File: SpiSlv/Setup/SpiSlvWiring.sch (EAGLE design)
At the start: 4 parts

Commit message: SpiSlv: changes for ^9
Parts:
- removed BM3: (no value), Documentation:RPUNO
- added BM1: (no value), Documentation:RPUNO
- D1: value GN -> RD
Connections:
- removed net 12V_SLA: BM3.BAT
- removed net 21V@200MA: BM3.PV
- removed net MOSI-MISO-SCK: BM3.SPI, U$1.SPI
- new net 12V8: BM1.PWR
- new net MOSI-MISO-SCK-CE0: BM1.SPI, U$1.SPI
- net !SS: now also BM1.ADC2_16, BM1.DIO10; no longer BM3.DIO10, BM3.DIO3
- net 5V-SMPS-ON-RPUPI: now also BM1.SHLD_VOUT; no longer BM3.SHLD_VOUT
- net N$1: now also BM1.CS0_EN5; no longer BM3.20MA@2
- net N$2: now also BM1.0V@3; no longer BM3.DIO4
- net N$5: now also BM1.RX; no longer BM3.RX
- net N$8: now also BM1.TX; no longer BM3.TX
- net SDA-SCL: now also BM1.I2C; no longer BM3.I2C
- net THRU-74LVC07: now also BM1.!RESET; no longer BM3.!RESET
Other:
- note added: "Note: nSS is active low hack: DIO16 used to operate nSS"
- note added: "hack"
- note removed: "Note: nSS is active low SPI will not work until it is active."
- moved on the sheet: D1

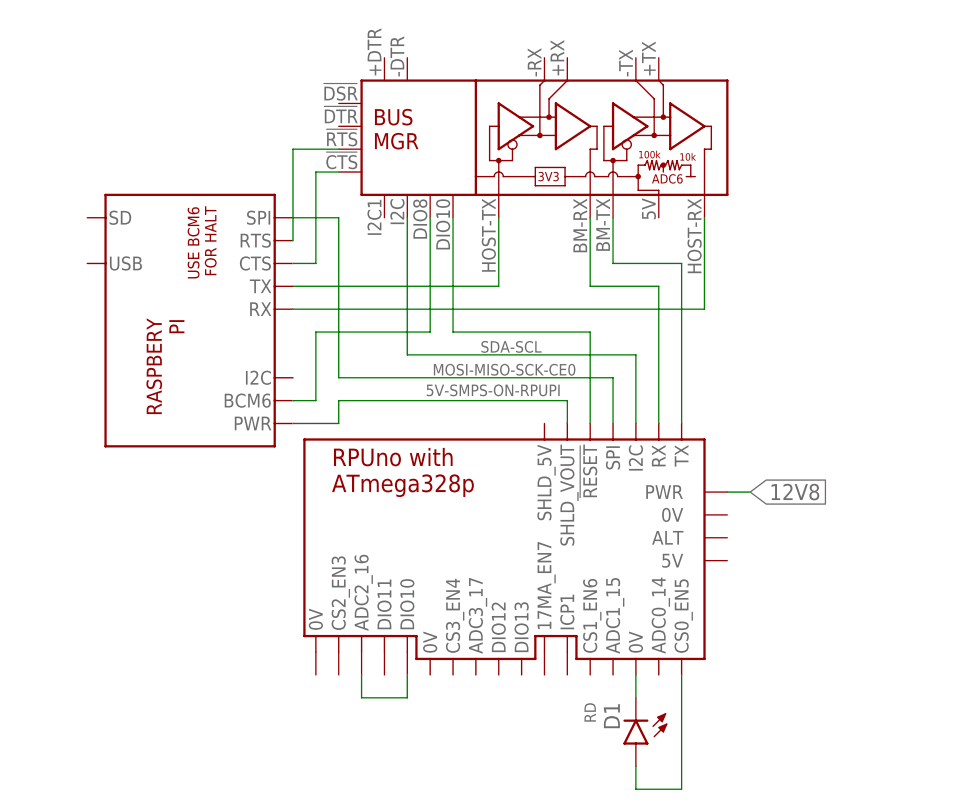
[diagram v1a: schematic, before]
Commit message: SpiSlv: remove ADC2 notes
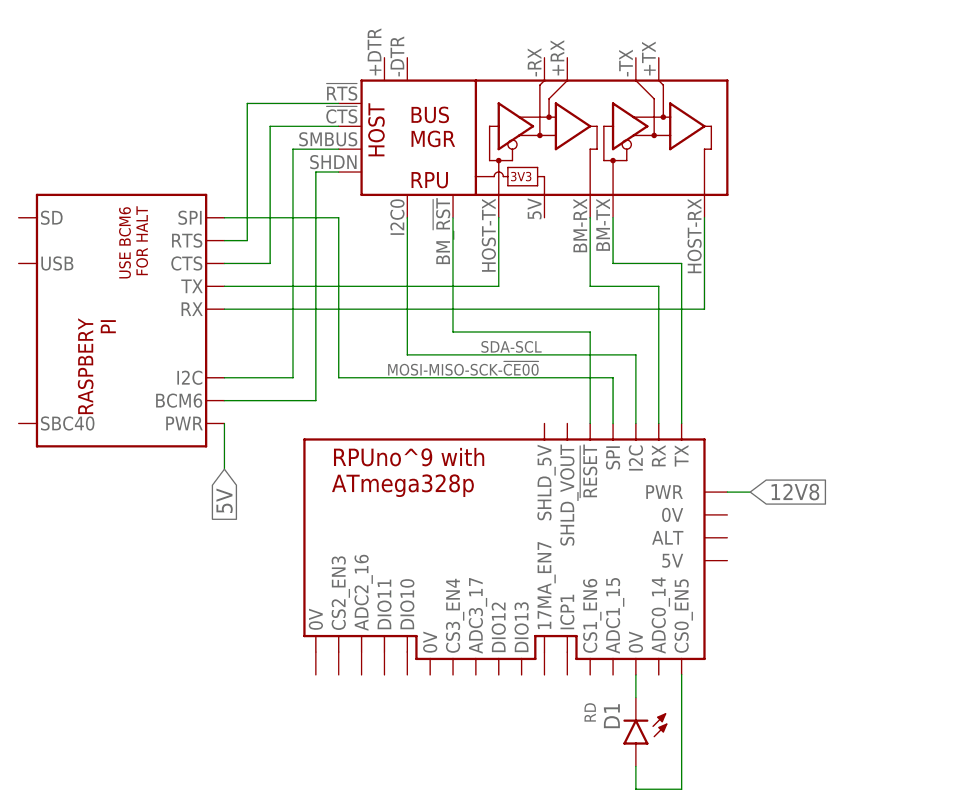
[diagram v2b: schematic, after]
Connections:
- net MOSI-MISO-SCK-CE0 renamed MOSI-MISO-SCK-!CE00
- removed net !SS: BM1.ADC2_16, BM1.DIO10
- removed net 5V-SMPS-ON-RPUPI: BM1.SHLD_VOUT, U$1.PWR
- new net 5V: U$1.PWR
- new net N$9: U$1.I2C, U$2.SMBUS
- net N$10: now also U$2.SHDN; no longer U$2.DIO8
- net SDA-SCL: now also U$2.I2C0; no longer U$2.I2C
- net THRU-74LVC07: now also U$2.BM-!RST!; no longer U$2.DIO10
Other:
- note removed: "Note: nSS is active low hack: DIO16 used to operate nSS"
- note removed: "hack"
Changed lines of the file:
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@@
 <text x="28.702" y="81.28" size="1.778" layer="98" rot="R90">MOSI</text>
 <text x="31.496" y="82.042" size="1.778" layer="98" rot="R90">nSS</text>
-<text x="17.78" y="73.66" size="1.778" layer="98">Note: nSS is active low
-hack: DIO16 used to operate nSS</text>
-<text x="19.558" y="88.138" size="1.778" layer="98">hack</text>
 </plain>
 <instances>
 <instance part="D1" gate="G$1" x="55.88" y="83.82" rot="R180"/>
-<instance part="U$1" gate="G$1" x="7.62" y="134.62" rot="R270"/>
+<instance part="U$1" gate="G$1" x="0" y="134.62" rot="R270"/>
 <instance part="U$2" gate="G$1" x="48.26" y="152.4"/>
 <instance part="BM1" gate="G$1" x="45.72" y="106.68"/>
@@
 </segment>
 </net>
-<net name="!SS" class="0">
-<segment>
-<pinref part="BM1" gate="G$1" pin="ADC2_16"/>
-<wire x1="25.4" y1="88.9" x2="25.4" y2="91.44" width="0.1524" layer="91"/>
-<pinref part="BM1" gate="G$1" pin="DIO10"/>
-<wire x1="25.4" y1="88.9" x2="30.48" y2="88.9" width="0.1524" layer="91"/>
-<wire x1="30.48" y1="88.9" x2="30.48" y2="91.44" width="0.1524" layer="91"/>
-</segment>
-</net>
 <net name="N$3" class="0">
 <segment>
 <pinref part="U$1" gate="G$1" pin="CTS"/>
-<wire x1="17.78" y1="137.16" x2="20.32" y2="137.16" width="0.1524" layer="91"/>
-<wire x1="20.32" y1="137.16" x2="20.32" y2="147.32" width="0.1524" layer="91"/>
+<wire x1="10.16" y1="137.16" x2="15.24" y2="137.16" width="0.1524" layer="91"/>
+<wire x1="15.24" y1="137.16" x2="15.24" y2="152.4" width="0.1524" layer="91"/>
 <pinref part="U$2" gate="G$1" pin="!CTS"/>
-<wire x1="20.32" y1="147.32" x2="22.86" y2="147.32" width="0.1524" layer="91"/>
-</segment>
-</net>
-<net name="N$4" class="0">
-<segment>
-<pinref part="U$1" gate="G$1" pin="RTS"/>
-<wire x1="17.78" y1="139.7" x2="17.78" y2="149.86" width="0.1524" layer="91"/>
-<pinref part="U$2" gate="G$1" pin="!RTS"/>
-<wire x1="17.78" y1="149.86" x2="22.86" y2="149.86" width="0.1524" layer="91"/>
+<wire x1="15.24" y1="152.4" x2="22.86" y2="152.4" width="0.1524" layer="91"/>
 </segment>
 </net>
 <net name="SDA-SCL" class="0">
 <segment>
-<pinref part="U$2" gate="G$1" pin="I2C"/>
+<pinref part="U$2" gate="G$1" pin="I2C0"/>
 <wire x1="30.48" y1="142.24" x2="30.48" y2="127" width="0.1524" layer="91"/>
 <wire x1="30.48" y1="127" x2="55.88" y2="127" width="0.1524" layer="91"/>
@@
 <wire x1="63.5" y1="142.24" x2="63.5" y2="132.08" width="0.1524" layer="91"/>
 <pinref part="U$1" gate="G$1" pin="RX"/>
-<wire x1="63.5" y1="132.08" x2="17.78" y2="132.08" width="0.1524" layer="91"/>
+<wire x1="63.5" y1="132.08" x2="10.16" y2="132.08" width="0.1524" layer="91"/>
 </segment>
 </net>
@@
 <wire x1="40.64" y1="142.24" x2="40.64" y2="134.62" width="0.1524" layer="91"/>
 <pinref part="U$1" gate="G$1" pin="TX"/>
-<wire x1="40.64" y1="134.62" x2="17.78" y2="134.62" width="0.1524" layer="91"/>
+<wire x1="40.64" y1="134.62" x2="10.16" y2="134.62" width="0.1524" layer="91"/>
 </segment>
 </net>
-<net name="MOSI-MISO-SCK-CE0" class="0">
+<net name="MOSI-MISO-SCK-!CE00" class="0">
 <segment>
 <pinref part="U$1" gate="G$1" pin="SPI"/>
-<wire x1="17.78" y1="142.24" x2="22.86" y2="142.24" width="0.1524" layer="91"/>
+<wire x1="10.16" y1="142.24" x2="22.86" y2="142.24" width="0.1524" layer="91"/>
 <wire x1="22.86" y1="142.24" x2="22.86" y2="124.46" width="0.1524" layer="91"/>
 <wire x1="22.86" y1="124.46" x2="53.34" y2="124.46" width="0.1524" layer="91"/>
 <wire x1="53.34" y1="124.46" x2="53.34" y2="119.38" width="0.1524" layer="91"/>
-<label x="33.274" y="124.714" size="1.27" layer="91"/>
+<label x="28.194" y="124.714" size="1.27" layer="91"/>
 <pinref part="BM1" gate="G$1" pin="SPI"/>
 </segment>
@@
 <segment>
 <pinref part="U$1" gate="G$1" pin="BCM6"/>
-<pinref part="U$2" gate="G$1" pin="DIO8"/>
-<wire x1="17.78" y1="121.92" x2="20.32" y2="121.92" width="0.1524" layer="91"/>
-<wire x1="20.32" y1="121.92" x2="20.32" y2="129.54" width="0.1524" layer="91"/>
-<wire x1="20.32" y1="129.54" x2="33.02" y2="129.54" width="0.1524" layer="91"/>
-<wire x1="33.02" y1="129.54" x2="33.02" y2="142.24" width="0.1524" layer="91"/>
+<wire x1="10.16" y1="121.92" x2="20.32" y2="121.92" width="0.1524" layer="91"/>
+<wire x1="20.32" y1="121.92" x2="20.32" y2="147.32" width="0.1524" layer="91"/>
+<pinref part="U$2" gate="G$1" pin="SHDN"/>
+<wire x1="20.32" y1="147.32" x2="22.86" y2="147.32" width="0.1524" layer="91"/>
 </segment>
 </net>
-<net name="5V-SMPS-ON-RPUPI" class="0">
+<net name="5V" class="0">
 <segment>
 <pinref part="U$1" gate="G$1" pin="PWR"/>
-<wire x1="17.78" y1="119.38" x2="22.86" y2="119.38" width="0.1524" layer="91"/>
-<wire x1="22.86" y1="119.38" x2="22.86" y2="121.92" width="0.1524" layer="91"/>
-<wire x1="22.86" y1="121.92" x2="48.26" y2="121.92" width="0.1524" layer="91"/>
-<wire x1="48.26" y1="121.92" x2="48.26" y2="119.38" width="0.1524" layer="91"/>
-<label x="32.512" y="122.428" size="1.27" layer="91"/>
-<pinref part="BM1" gate="G$1" pin="SHLD_VOUT"/>
+<wire x1="10.16" y1="119.38" x2="10.16" y2="114.3" width="0.1524" layer="91"/>
+<label x="10.16" y="114.3" size="1.778" layer="91" rot="R270" xref="yes"/>
 </segment>
 </net>
 <net name="THRU-74LVC07" class="0">
 <segment>
-<pinref part="U$2" gate="G$1" pin="DIO10"/>
+<pinref part="U$2" gate="G$1" pin="BM-!RST!"/>
 <wire x1="35.56" y1="142.24" x2="35.56" y2="129.54" width="0.1524" layer="91"/>
 <wire x1="35.56" y1="129.54" x2="50.8" y2="129.54" width="0.1524" layer="91"/>
@@
 </segment>
 </net>
+<net name="N$4" class="0">
+<segment>
+<pinref part="U$2" gate="G$1" pin="!RTS"/>
+<wire x1="22.86" y1="154.94" x2="12.7" y2="154.94" width="0.1524" layer="91"/>
+<wire x1="12.7" y1="154.94" x2="12.7" y2="139.7" width="0.1524" layer="91"/>
+<pinref part="U$1" gate="G$1" pin="RTS"/>
+<wire x1="12.7" y1="139.7" x2="10.16" y2="139.7" width="0.1524" layer="91"/>
+</segment>
+</net>
+<net name="N$9" class="0">
+<segment>
+<pinref part="U$2" gate="G$1" pin="SMBUS"/>
+<pinref part="U$1" gate="G$1" pin="I2C"/>
+<wire x1="10.16" y1="124.46" x2="17.78" y2="124.46" width="0.1524" layer="91"/>
+<wire x1="17.78" y1="124.46" x2="17.78" y2="149.86" width="0.1524" layer="91"/>
+<wire x1="17.78" y1="149.86" x2="22.86" y2="149.86" width="0.1524" layer="91"/>
+</segment>
+</net>
